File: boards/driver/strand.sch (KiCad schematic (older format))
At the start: 5 parts, among them Q4 MMBT2907

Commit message: Driver board: a bit more schematic work and some initial footprint selections
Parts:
- R74, R75, R76: footprint Resistor_SMD:R_1206_3216Metric -> Resistor_SMD:R_0603_1608Metric
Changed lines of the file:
@@
 F 0 "R91" H 5368 3846 50  0000 L CNN
 F 1 "2k" H 5368 3755 50  0000 L CNN
-F 2 "Resistor_SMD:R_1206_3216Metric" V 5340 3790 50  0001 C CNN
+F 2 "Resistor_SMD:R_0603_1608Metric" V 5340 3790 50  0001 C CNN
 F 3 "~" H 5300 3800 50  0001 C CNN
 	1    5300 3800
@@
 F 0 "R90" H 5368 3396 50  0000 L CNN
 F 1 "5.1k" H 5368 3305 50  0000 L CNN
-F 2 "Resistor_SMD:R_1206_3216Metric" V 5340 3340 50  0001 C CNN
+F 2 "Resistor_SMD:R_0603_1608Metric" V 5340 3340 50  0001 C CNN
 F 3 "~" H 5300 3350 50  0001 C CNN
 	1    5300 3350
@@
 F 0 "R92" H 5968 4096 50  0000 L CNN
 F 1 "3k" H 5968 4005 50  0000 L CNN
-F 2 "Resistor_SMD:R_1206_3216Metric" V 5940 4040 50  0001 C CNN
+F 2 "Resistor_SMD:R_0603_1608Metric" V 5940 4040 50  0001 C CNN
 F 3 "~" H 5900 4050 50  0001 C CNN
 	1    5900 4050

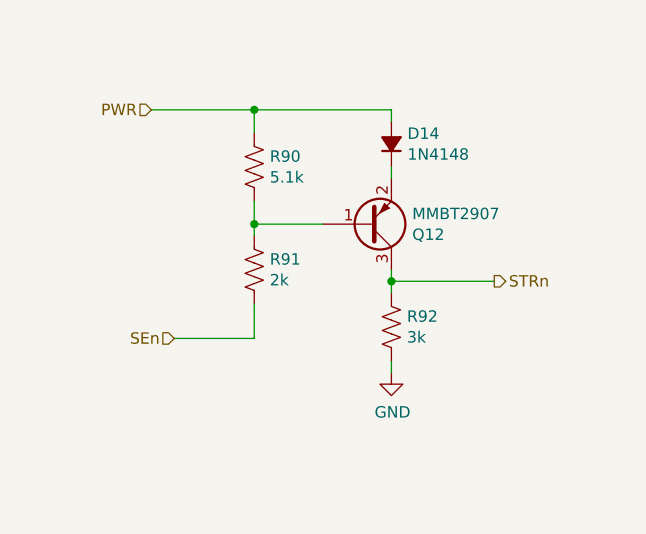
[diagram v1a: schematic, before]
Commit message: Driver board: finished first rough draft schematic. Lots of placeholders, but at least every place is held.
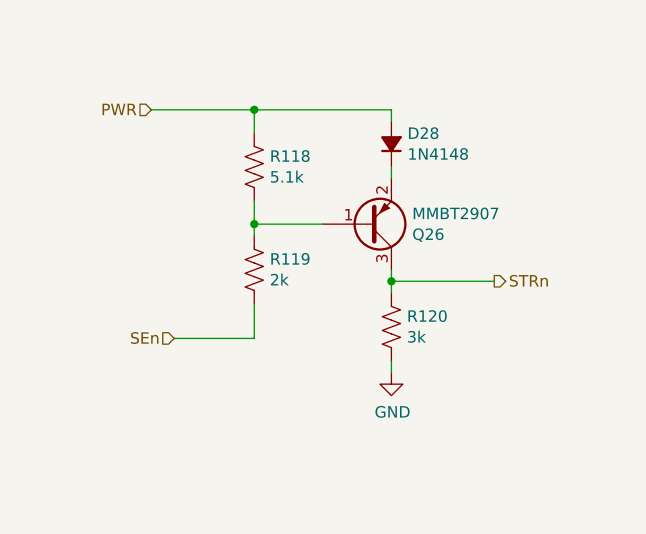
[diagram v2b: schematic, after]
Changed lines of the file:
@@
 $Descr A4 11693 8268
 encoding utf-8
-Sheet 15 68
+Sheet 15 69
 Title ""
 Date ""
@@
 AR Path="/64D2DF1E/618ABD52/6189080E" Ref="R115"  Part="1"
 AR Path="/64D2DF1E/618ABD61/6189080E" Ref="R119"  Part="1"
-F 0 "R91" H 5368 3846 50  0000 L CNN
+F 0 "R119" H 5368 3846 50  0000 L CNN
 F 1 "2k" H 5368 3755 50  0000 L CNN
 F 2 "Resistor_SMD:R_0603_1608Metric" V 5340 3790 50  0001 C CNN
@@
 AR Path="/64D2DF1E/618ABD52/61890815" Ref="R114"  Part="1"
 AR Path="/64D2DF1E/618ABD61/61890815" Ref="R118"  Part="1"
-F 0 "R90" H 5368 3396 50  0000 L CNN
+F 0 "R118" H 5368 3396 50  0000 L CNN
 F 1 "5.1k" H 5368 3305 50  0000 L CNN
 F 2 "Resistor_SMD:R_0603_1608Metric" V 5340 3340 50  0001 C CNN
@@
 AR Path="/64D2DF1E/618ABD52/6189081E" Ref="Q24"  Part="1"
 AR Path="/64D2DF1E/618ABD61/6189081E" Ref="Q26"  Part="1"
-F 0 "Q12" H 5991 3646 50  0000 L CNN
+F 0 "Q26" H 5991 3646 50  0000 L CNN
 F 1 "MMBT2907" H 5991 3555 50  0000 L CNN
 F 2 "Package_TO_SOT_SMD:SOT-23" H 6000 3700 50  0001 C CNN
@@
 AR Path="/64D2DF1E/618ABD52/6189082B" Ref="R116"  Part="1"
 AR Path="/64D2DF1E/618ABD61/6189082B" Ref="R120"  Part="1"
-F 0 "R92" H 5968 4096 50  0000 L CNN
+F 0 "R120" H 5968 4096 50  0000 L CNN
 F 1 "3k" H 5968 4005 50  0000 L CNN
 F 2 "Resistor_SMD:R_0603_1608Metric" V 5940 4040 50  0001 C CNN
@@
 AR Path="/64D2DF1E/618ABD52/61890838" Ref="D26"  Part="1"
 AR Path="/64D2DF1E/618ABD61/61890838" Ref="D28"  Part="1"
-F 0 "D14" V 5946 3180 50  0000 R CNN
+F 0 "D28" V 5946 3180 50  0000 R CNN
 F 1 "1N4148" V 5855 3180 50  0000 R CNN
 F 2 "Diode_SMD:D_SOD-323" V 5900 3250 50  0001 C CNN

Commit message: Driver board: fleshed out the hotswap controller, tweaked some resistors, and added some bypass caps
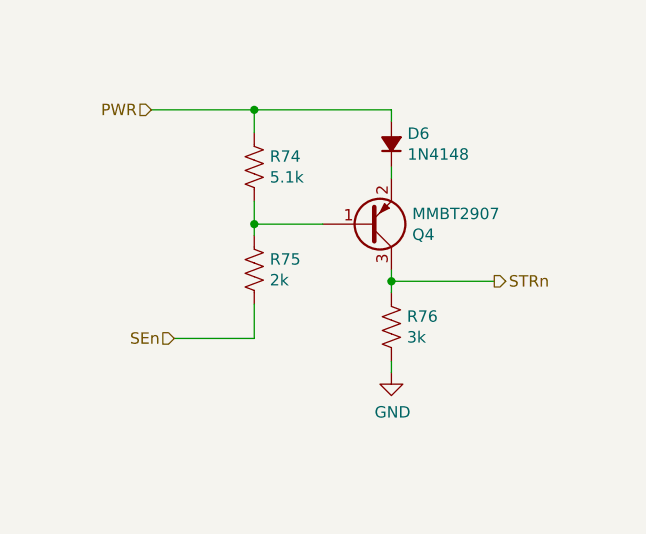
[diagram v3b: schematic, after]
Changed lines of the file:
@@
 $Descr A4 11693 8268
 encoding utf-8
-Sheet 15 69
+Sheet 7 69
 Title ""
 Date ""
@@
 AR Path="/64D2DF1E/618ABD52/6189080E" Ref="R115"  Part="1"
 AR Path="/64D2DF1E/618ABD61/6189080E" Ref="R119"  Part="1"
-F 0 "R119" H 5368 3846 50  0000 L CNN
+F 0 "R75" H 5368 3846 50  0000 L CNN
 F 1 "2k" H 5368 3755 50  0000 L CNN
 F 2 "Resistor_SMD:R_0603_1608Metric" V 5340 3790 50  0001 C CNN
@@
 AR Path="/64D2DF1E/618ABD52/61890815" Ref="R114"  Part="1"
 AR Path="/64D2DF1E/618ABD61/61890815" Ref="R118"  Part="1"
-F 0 "R118" H 5368 3396 50  0000 L CNN
+F 0 "R74" H 5368 3396 50  0000 L CNN
 F 1 "5.1k" H 5368 3305 50  0000 L CNN
 F 2 "Resistor_SMD:R_0603_1608Metric" V 5340 3340 50  0001 C CNN
@@
 AR Path="/64D2DF1E/618ABD52/6189081E" Ref="Q24"  Part="1"
 AR Path="/64D2DF1E/618ABD61/6189081E" Ref="Q26"  Part="1"
-F 0 "Q26" H 5991 3646 50  0000 L CNN
+F 0 "Q4" H 5991 3646 50  0000 L CNN
 F 1 "MMBT2907" H 5991 3555 50  0000 L CNN
 F 2 "Package_TO_SOT_SMD:SOT-23" H 6000 3700 50  0001 C CNN
@@
 AR Path="/64D2DF1E/618ABD52/6189082B" Ref="R116"  Part="1"
 AR Path="/64D2DF1E/618ABD61/6189082B" Ref="R120"  Part="1"
-F 0 "R120" H 5968 4096 50  0000 L CNN
+F 0 "R76" H 5968 4096 50  0000 L CNN
 F 1 "3k" H 5968 4005 50  0000 L CNN
 F 2 "Resistor_SMD:R_0603_1608Metric" V 5940 4040 50  0001 C CNN
@@
 AR Path="/64D2DF1E/618ABD52/61890838" Ref="D26"  Part="1"
 AR Path="/64D2DF1E/618ABD61/61890838" Ref="D28"  Part="1"
-F 0 "D28" V 5946 3180 50  0000 R CNN
+F 0 "D6" V 5946 3180 50  0000 R CNN
 F 1 "1N4148" V 5855 3180 50  0000 R CNN
 F 2 "Diode_SMD:D_SOD-323" V 5900 3250 50  0001 C CNN
@@
 	5900 3850 5900 3900
 $Comp
-L power:GND #PWR038
+L power:GND #PWR041
 U 1 1 6188E8C0
 P 5900 4250
-AR Path="/64D2DF1E/61886B73/6188E8C0" Ref="#PWR038"  Part="1"
-AR Path="/64D2DF1E/6189F177/6188E8C0" Ref="#PWR040"  Part="1"
-AR Path="/64D2DF1E/618A142B/6188E8C0" Ref="#PWR042"  Part="1"
-AR Path="/64D2DF1E/618A143A/6188E8C0" Ref="#PWR044"  Part="1"
-AR Path="/64D2DF1E/618A4047/6188E8C0" Ref="#PWR046"  Part="1"
-AR Path="/64D2DF1E/618A4056/6188E8C0" Ref="#PWR048"  Part="1"
-AR Path="/64D2DF1E/618A4065/6188E8C0" Ref="#PWR050"  Part="1"
-AR Path="/64D2DF1E/618A4074/6188E8C0" Ref="#PWR052"  Part="1"
-AR Path="/64D2DF1E/618ABD34/6188E8C0" Ref="#PWR054"  Part="1"
-AR Path="/64D2DF1E/618ABD43/6188E8C0" Ref="#PWR056"  Part="1"
-AR Path="/64D2DF1E/618ABD52/6188E8C0" Ref="#PWR058"  Part="1"
-AR Path="/64D2DF1E/618ABD61/6188E8C0" Ref="#PWR060"  Part="1"
-F 0 "#PWR060" H 5900 4000 50  0001 C CNN
+AR Path="/64D2DF1E/61886B73/6188E8C0" Ref="#PWR041"  Part="1"
+AR Path="/64D2DF1E/6189F177/6188E8C0" Ref="#PWR043"  Part="1"
+AR Path="/64D2DF1E/618A142B/6188E8C0" Ref="#PWR045"  Part="1"
+AR Path="/64D2DF1E/618A143A/6188E8C0" Ref="#PWR047"  Part="1"
+AR Path="/64D2DF1E/618A4047/6188E8C0" Ref="#PWR049"  Part="1"
+AR Path="/64D2DF1E/618A4056/6188E8C0" Ref="#PWR051"  Part="1"
+AR Path="/64D2DF1E/618A4065/6188E8C0" Ref="#PWR053"  Part="1"
+AR Path="/64D2DF1E/618A4074/6188E8C0" Ref="#PWR055"  Part="1"
+AR Path="/64D2DF1E/618ABD34/6188E8C0" Ref="#PWR057"  Part="1"
+AR Path="/64D2DF1E/618ABD43/6188E8C0" Ref="#PWR059"  Part="1"
+AR Path="/64D2DF1E/618ABD52/6188E8C0" Ref="#PWR061"  Part="1"
+AR Path="/64D2DF1E/618ABD61/6188E8C0" Ref="#PWR063"  Part="1"
+F 0 "#PWR041" H 5900 4000 50  0001 C CNN
 F 1 "GND" H 5905 4077 50  0000 C CNN
 F 2 "" H 5900 4250 50  0001 C CNN

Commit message: Driver board: significant cleanup. Moved sense amp pairs into a subsheet, split tuning resistors into two globally, pushed input circuits into their corresponding sheets.
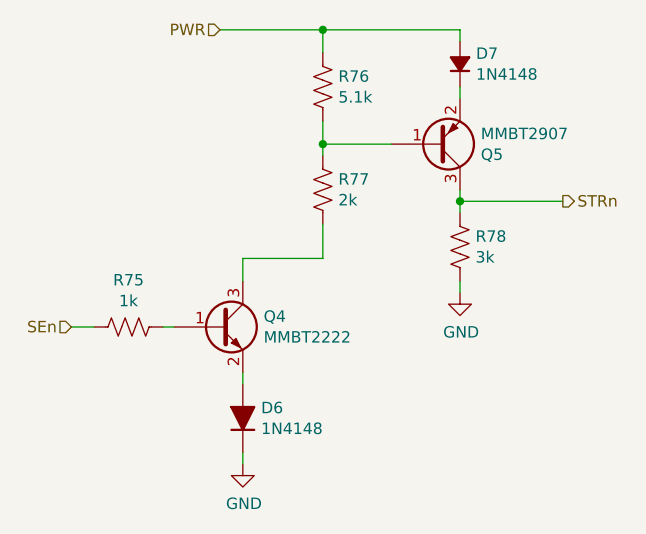
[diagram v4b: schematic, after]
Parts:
- added D6: 1N4148, Diode_SMD:D_SOD-323, symbol Device:D_ALT
- added Q4: MMBT2222, Package_TO_SOT_SMD:SOT-23, symbol Device:Q_NPN_BEC
- added R75: 1k, Resistor_SMD:R_0603_1608Metric, symbol Device:R_US
- renumbered D6 to D7, Q4 to Q5, R74 to R76, R75 to R77, R76 to R78
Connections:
- net GND: now also D6.1 (K)
- net SEn: now also R75.2; no longer R77.2
- new net: Q4.3 (C), R77.2
- new net: Q4.1 (B), R75.1
- new net: D6.2 (A), Q4.2 (E)
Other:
- moved on the sheet: D7, Q5, R76, R77, R78

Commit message: Driver board: integrated DIN 41612 backplane connector, and made a dedicated parity inhibit sheet with a different set resistor value.
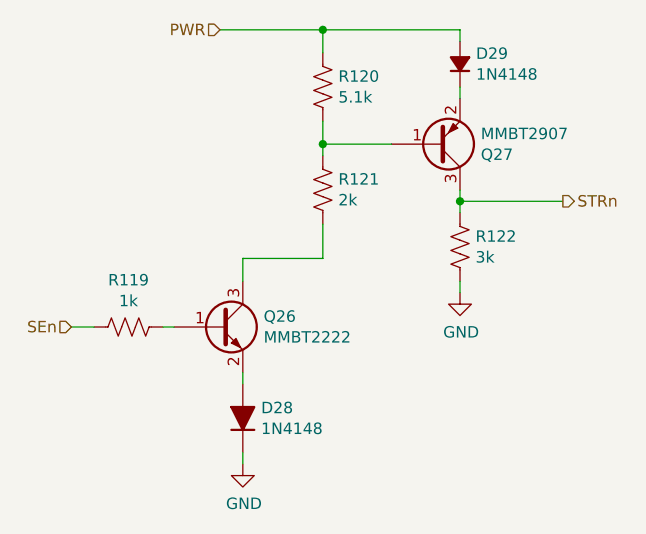
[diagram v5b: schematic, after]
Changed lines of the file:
@@
 AR Path="/64D2DF1E/618ABD52/6189080E" Ref="R117"  Part="1"
 AR Path="/64D2DF1E/618ABD61/6189080E" Ref="R121"  Part="1"
-F 0 "R77" H 5668 3496 50  0000 L CNN
+F 0 "R121" H 5668 3496 50  0000 L CNN
 F 1 "2k" H 5668 3405 50  0000 L CNN
 F 2 "Resistor_SMD:R_0603_1608Metric" V 5640 3440 50  0001 C CNN
@@
 AR Path="/64D2DF1E/618ABD52/61890815" Ref="R116"  Part="1"
 AR Path="/64D2DF1E/618ABD61/61890815" Ref="R120"  Part="1"
-F 0 "R76" H 5668 3046 50  0000 L CNN
+F 0 "R120" H 5668 3046 50  0000 L CNN
 F 1 "5.1k" H 5668 2955 50  0000 L CNN
 F 2 "Resistor_SMD:R_0603_1608Metric" V 5640 2990 50  0001 C CNN
@@
 AR Path="/64D2DF1E/618ABD52/6189081E" Ref="Q25"  Part="1"
 AR Path="/64D2DF1E/618ABD61/6189081E" Ref="Q27"  Part="1"
-F 0 "Q5" H 6291 3296 50  0000 L CNN
+F 0 "Q27" H 6291 3296 50  0000 L CNN
 F 1 "MMBT2907" H 6291 3205 50  0000 L CNN
 F 2 "Package_TO_SOT_SMD:SOT-23" H 6300 3350 50  0001 C CNN
@@
 AR Path="/64D2DF1E/618ABD52/6189082B" Ref="R118"  Part="1"
 AR Path="/64D2DF1E/618ABD61/6189082B" Ref="R122"  Part="1"
-F 0 "R78" H 6268 3746 50  0000 L CNN
+F 0 "R122" H 6268 3746 50  0000 L CNN
 F 1 "3k" H 6268 3655 50  0000 L CNN
 F 2 "Resistor_SMD:R_0603_1608Metric" V 6240 3690 50  0001 C CNN
@@
 AR Path="/64D2DF1E/618ABD52/61890838" Ref="D27"  Part="1"
 AR Path="/64D2DF1E/618ABD61/61890838" Ref="D29"  Part="1"
-F 0 "D7" V 6246 2830 50  0000 R CNN
+F 0 "D29" V 6246 2830 50  0000 R CNN
 F 1 "1N4148" V 6155 2830 50  0000 R CNN
 F 2 "Diode_SMD:D_SOD-323" V 6200 2900 50  0001 C CNN
@@
 	6200 3500 6200 3550
 $Comp
-L power:GND #PWR059
+L power:GND #PWR060
 U 1 1 6188E8C0
 P 6200 3900
-AR Path="/64D2DF1E/61886B73/6188E8C0" Ref="#PWR059"  Part="1"
-AR Path="/64D2DF1E/6189F177/6188E8C0" Ref="#PWR061"  Part="1"
-AR Path="/64D2DF1E/618A142B/6188E8C0" Ref="#PWR063"  Part="1"
-AR Path="/64D2DF1E/618A143A/6188E8C0" Ref="#PWR065"  Part="1"
-AR Path="/64D2DF1E/618A4047/6188E8C0" Ref="#PWR067"  Part="1"
-AR Path="/64D2DF1E/618A4056/6188E8C0" Ref="#PWR069"  Part="1"
-AR Path="/64D2DF1E/618A4065/6188E8C0" Ref="#PWR071"  Part="1"
-AR Path="/64D2DF1E/618A4074/6188E8C0" Ref="#PWR073"  Part="1"
-AR Path="/64D2DF1E/618ABD34/6188E8C0" Ref="#PWR075"  Part="1"
-AR Path="/64D2DF1E/618ABD43/6188E8C0" Ref="#PWR077"  Part="1"
-AR Path="/64D2DF1E/618ABD52/6188E8C0" Ref="#PWR079"  Part="1"
-AR Path="/64D2DF1E/618ABD61/6188E8C0" Ref="#PWR081"  Part="1"
-F 0 "#PWR059" H 6200 3650 50  0001 C CNN
+AR Path="/64D2DF1E/61886B73/6188E8C0" Ref="#PWR060"  Part="1"
+AR Path="/64D2DF1E/6189F177/6188E8C0" Ref="#PWR062"  Part="1"
+AR Path="/64D2DF1E/618A142B/6188E8C0" Ref="#PWR064"  Part="1"
+AR Path="/64D2DF1E/618A143A/6188E8C0" Ref="#PWR066"  Part="1"
+AR Path="/64D2DF1E/618A4047/6188E8C0" Ref="#PWR068"  Part="1"
+AR Path="/64D2DF1E/618A4056/6188E8C0" Ref="#PWR070"  Part="1"
+AR Path="/64D2DF1E/618A4065/6188E8C0" Ref="#PWR072"  Part="1"
+AR Path="/64D2DF1E/618A4074/6188E8C0" Ref="#PWR074"  Part="1"
+AR Path="/64D2DF1E/618ABD34/6188E8C0" Ref="#PWR076"  Part="1"
+AR Path="/64D2DF1E/618ABD43/6188E8C0" Ref="#PWR078"  Part="1"
+AR Path="/64D2DF1E/618ABD52/6188E8C0" Ref="#PWR080"  Part="1"
+AR Path="/64D2DF1E/618ABD61/6188E8C0" Ref="#PWR082"  Part="1"
+F 0 "#PWR082" H 6200 3650 50  0001 C CNN
 F 1 "GND" H 6205 3727 50  0000 C CNN
 F 2 "" H 6200 3900 50  0001 C CNN
@@
 AR Path="/64D2DF1E/618ABD52/639DBFB4" Ref="R115"  Part="1"
 AR Path="/64D2DF1E/618ABD61/639DBFB4" Ref="R119"  Part="1"
-F 0 "R75" V 4545 4050 50  0000 C CNN
+F 0 "R119" V 4545 4050 50  0000 C CNN
 F 1 "1k" V 4636 4050 50  0000 C CNN
 F 2 "Resistor_SMD:R_0603_1608Metric" V 4790 4040 50  0001 C CNN
@@
 AR Path="/64D2DF1E/618ABD52/639DBFBA" Ref="Q24"  Part="1"
 AR Path="/64D2DF1E/618ABD61/639DBFBA" Ref="Q26"  Part="1"
-F 0 "Q4" H 5341 4096 50  0000 L CNN
+F 0 "Q26" H 5341 4096 50  0000 L CNN
 F 1 "MMBT2222" H 5341 4005 50  0000 L CNN
 F 2 "Package_TO_SOT_SMD:SOT-23" H 5350 4150 50  0001 C CNN
@@
 AR Path="/64D2DF1E/618ABD52/639DBFC4" Ref="D26"  Part="1"
 AR Path="/64D2DF1E/618ABD61/639DBFC4" Ref="D28"  Part="1"
-F 0 "D6" V 5296 4370 50  0000 R CNN
+F 0 "D28" V 5296 4370 50  0000 R CNN
 F 1 "1N4148" V 5205 4370 50  0000 R CNN
 F 2 "Diode_SMD:D_SOD-323" H 5250 4450 50  0001 C CNN
@@
 AR Path="/64D2DF1E/618ABD5A/639DBFCC" Ref="#PWR?"  Part="1"
 AR Path="/64D2DF1E/618ABD69/639DBFCC" Ref="#PWR?"  Part="1"
-AR Path="/64D2DF1E/61886B73/639DBFCC" Ref="#PWR058"  Part="1"
-AR Path="/64D2DF1E/6189F177/639DBFCC" Ref="#PWR060"  Part="1"
-AR Path="/64D2DF1E/618A142B/639DBFCC" Ref="#PWR062"  Part="1"
-AR Path="/64D2DF1E/618A143A/639DBFCC" Ref="#PWR064"  Part="1"
-AR Path="/64D2DF1E/618A4047/639DBFCC" Ref="#PWR066"  Part="1"
-AR Path="/64D2DF1E/618A4056/639DBFCC" Ref="#PWR068"  Part="1"
-AR Path="/64D2DF1E/618A4065/639DBFCC" Ref="#PWR070"  Part="1"
-AR Path="/64D2DF1E/618A4074/639DBFCC" Ref="#PWR072"  Part="1"
-AR Path="/64D2DF1E/618ABD34/639DBFCC" Ref="#PWR074"  Part="1"
-AR Path="/64D2DF1E/618ABD43/639DBFCC" Ref="#PWR076"  Part="1"
-AR Path="/64D2DF1E/618ABD52/639DBFCC" Ref="#PWR078"  Part="1"
-AR Path="/64D2DF1E/618ABD61/639DBFCC" Ref="#PWR080"  Part="1"
-F 0 "#PWR058" H 5250 4400 50  0001 C CNN
+AR Path="/64D2DF1E/61886B73/639DBFCC" Ref="#PWR059"  Part="1"
+AR Path="/64D2DF1E/6189F177/639DBFCC" Ref="#PWR061"  Part="1"
+AR Path="/64D2DF1E/618A142B/639DBFCC" Ref="#PWR063"  Part="1"
+AR Path="/64D2DF1E/618A143A/639DBFCC" Ref="#PWR065"  Part="1"
+AR Path="/64D2DF1E/618A4047/639DBFCC" Ref="#PWR067"  Part="1"
+AR Path="/64D2DF1E/618A4056/639DBFCC" Ref="#PWR069"  Part="1"
+AR Path="/64D2DF1E/618A4065/639DBFCC" Ref="#PWR071"  Part="1"
+AR Path="/64D2DF1E/618A4074/639DBFCC" Ref="#PWR073"  Part="1"
+AR Path="/64D2DF1E/618ABD34/639DBFCC" Ref="#PWR075"  Part="1"
+AR Path="/64D2DF1E/618ABD43/639DBFCC" Ref="#PWR077"  Part="1"
+AR Path="/64D2DF1E/618ABD52/639DBFCC" Ref="#PWR079"  Part="1"
+AR Path="/64D2DF1E/618ABD61/639DBFCC" Ref="#PWR081"  Part="1"
+F 0 "#PWR081" H 5250 4400 50  0001 C CNN
 F 1 "GND" H 5255 4477 50  0000 C CNN
 F 2 "" H 5250 4650 50  0001 C CNN

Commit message: Driver board: largely fleshed out part selection
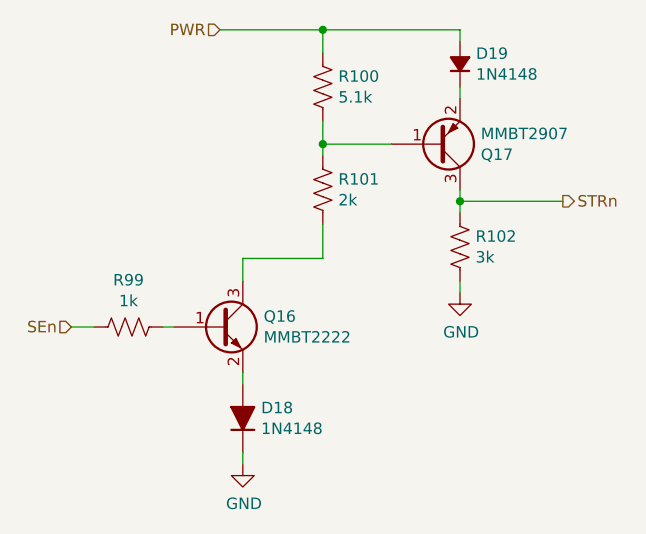
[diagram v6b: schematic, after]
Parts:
- D6, D7: Digikey (none) -> https://www.digikey.com/en/products/detail/smc-diode-soluti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; Part Number (none) -> 1N4148WSTR
- Q4: Digikey (none) -> https://www.digikey.com/en/products/detail/MMBT2222A-G/641-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; Part Number (none) -> MMBT2222A-G
- Q5: Digikey (none) -> https://www.digikey.com/en/products/detail/MMBT2907A-G/641-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; Part Number (none) -> MMBT2907A-G
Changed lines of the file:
@@
 $Descr A4 11693 8268
 encoding utf-8
-Sheet 14 64
+Sheet 20 64
 Title ""
 Date ""
@@
 AR Path="/64D2DF1E/618ABD52/6189080E" Ref="R117"  Part="1"
 AR Path="/64D2DF1E/618ABD61/6189080E" Ref="R121"  Part="1"
-F 0 "R121" H 5668 3496 50  0000 L CNN
+F 0 "R101" H 5668 3496 50  0000 L CNN
 F 1 "2k" H 5668 3405 50  0000 L CNN
 F 2 "Resistor_SMD:R_0603_1608Metric" V 5640 3440 50  0001 C CNN
@@
 AR Path="/64D2DF1E/618ABD52/61890815" Ref="R116"  Part="1"
 AR Path="/64D2DF1E/618ABD61/61890815" Ref="R120"  Part="1"
-F 0 "R120" H 5668 3046 50  0000 L CNN
+F 0 "R100" H 5668 3046 50  0000 L CNN
 F 1 "5.1k" H 5668 2955 50  0000 L CNN
 F 2 "Resistor_SMD:R_0603_1608Metric" V 5640 2990 50  0001 C CNN
@@
 AR Path="/64D2DF1E/618ABD52/6189081E" Ref="Q25"  Part="1"
 AR Path="/64D2DF1E/618ABD61/6189081E" Ref="Q27"  Part="1"
-F 0 "Q27" H 6291 3296 50  0000 L CNN
+F 0 "Q17" H 6291 3296 50  0000 L CNN
 F 1 "MMBT2907" H 6291 3205 50  0000 L CNN
 F 2 "Package_TO_SOT_SMD:SOT-23" H 6300 3350 50  0001 C CNN
 F 3 "~" H 6100 3250 50  0001 C CNN
+F 4 "https://www.digikey.com/en/products/detail/MMBT2907A-G/641-1952-1-ND/9477883" H 6100 3250 50  0001 C CNN "Digikey"
+F 5 "MMBT2907A-G" H 6100 3250 50  0001 C CNN "Part Number"
 	1    6100 3250
 	1    0    0    1
@@
 AR Path="/64D2DF1E/618ABD52/6189082B" Ref="R118"  Part="1"
 AR Path="/64D2DF1E/618ABD61/6189082B" Ref="R122"  Part="1"
-F 0 "R122" H 6268 3746 50  0000 L CNN
+F 0 "R102" H 6268 3746 50  0000 L CNN
 F 1 "3k" H 6268 3655 50  0000 L CNN
 F 2 "Resistor_SMD:R_0603_1608Metric" V 6240 3690 50  0001 C CNN
@@
 AR Path="/64D2DF1E/618ABD52/61890838" Ref="D27"  Part="1"
 AR Path="/64D2DF1E/618ABD61/61890838" Ref="D29"  Part="1"
-F 0 "D29" V 6246 2830 50  0000 R CNN
+F 0 "D19" V 6246 2830 50  0000 R CNN
 F 1 "1N4148" V 6155 2830 50  0000 R CNN
 F 2 "Diode_SMD:D_SOD-323" V 6200 2900 50  0001 C CNN
 F 3 "~" V 6200 2900 50  0001 C CNN
+F 4 "1N4148WSTR" V 4900 3150 50  0001 C CNN "Part Number"
+F 5 "https://www.digikey.com/en/products/detail/smc-diode-solutions/1N4148WSTR/6022449" V 4900 3150 50  0001 C CNN "Digikey"
 	1    6200 2900
 	0    -1   -1   0
@@
 AR Path="/64D2DF1E/618ABD52/639DBFB4" Ref="R115"  Part="1"
 AR Path="/64D2DF1E/618ABD61/639DBFB4" Ref="R119"  Part="1"
-F 0 "R119" V 4545 4050 50  0000 C CNN
+F 0 "R99" V 4545 4050 50  0000 C CNN
 F 1 "1k" V 4636 4050 50  0000 C CNN
 F 2 "Resistor_SMD:R_0603_1608Metric" V 4790 4040 50  0001 C CNN
@@
 AR Path="/64D2DF1E/618ABD52/639DBFBA" Ref="Q24"  Part="1"
 AR Path="/64D2DF1E/618ABD61/639DBFBA" Ref="Q26"  Part="1"
-F 0 "Q26" H 5341 4096 50  0000 L CNN
+F 0 "Q16" H 5341 4096 50  0000 L CNN
 F 1 "MMBT2222" H 5341 4005 50  0000 L CNN
 F 2 "Package_TO_SOT_SMD:SOT-23" H 5350 4150 50  0001 C CNN
 F 3 "~" H 5150 4050 50  0001 C CNN
+F 4 "https://www.digikey.com/en/products/detail/MMBT2222A-G/641-1942-1-ND/9477875" H 5150 4050 50  0001 C CNN "Digikey"
+F 5 "MMBT2222A-G" H 5150 4050 50  0001 C CNN "Part Number"
 	1    5150 4050
 	1    0    0    -1
@@
 AR Path="/64D2DF1E/618ABD52/639DBFC4" Ref="D26"  Part="1"
 AR Path="/64D2DF1E/618ABD61/639DBFC4" Ref="D28"  Part="1"
-F 0 "D28" V 5296 4370 50  0000 R CNN
+F 0 "D18" V 5296 4370 50  0000 R CNN
 F 1 "1N4148" V 5205 4370 50  0000 R CNN
 F 2 "Diode_SMD:D_SOD-323" H 5250 4450 50  0001 C CNN
 F 3 "~" H 5250 4450 50  0001 C CNN
+F 4 "1N4148WSTR" V 4900 3150 50  0001 C CNN "Part Number"
+F 5 "https://www.digikey.com/en/products/detail/smc-diode-solutions/1N4148WSTR/6022449" V 4900 3150 50  0001 C CNN "Digikey"
 	1    5250 4450
 	0    -1   -1   0
